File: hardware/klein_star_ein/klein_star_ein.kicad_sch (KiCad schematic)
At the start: 184 parts, among them J1 USB_A, J10 AudioJack3_Ground_Switch, J11 AudioJack3_Ground_Switch, J12 AudioJack3_Ground_Switch, J2 DB15_Female_HighDensity_Mount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, J3 Bus_PCI_Express_x1, J4 1367073-1, J5 RJ45_LED_Shielded, J6 USB_C_Receptacle, J7 MEM2051-00-195-00-A, J8 AudioJack3_Ground_Switch, J9 AudioJack3_Ground_Switch, U1 ECP5UM25, U10 SN74ALVC245PWR, U11 KSZ9021RL, U12 TUSB2036, U13 TPS2041B, U2 MT41K512M16, U3 MT41K512M16, U4 FT2232HQ, U5 W25Q128JVS, U6 USB3300-EZK, U7 USB3300-EZK, U8 SN74ALVC245PWR, U9 SN74ALVC245PWR

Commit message: ech
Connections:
- net +1V35: no longer U1.L14 (VCCIO3/-), U1.L15 (VCCIO3/-), U1.M15 (VCCIO3/-)
- net DRAM_ADDR_0: no longer U1.E17 (PR5B/RDQ8/-)
- net DRAM_ADDR_1: no longer U1.T18 (PR44D/RDQ44/-)
- net DRAM_ADDR_10: no longer U1.U16 (PR47C/RDQ44/LRC_GPLL0T_IN)
- net DRAM_ADDR_11: no longer U1.R17 (PR35D/RDQ32/-)
- net DRAM_ADDR_12: now also RN7.2 (R2.1); no longer RN8.4 (R4.1), U1.U18 (PR47A/RDQ44/-)
- net DRAM_ADDR_13: no longer U1.J16 (PR11D/RDQ8/-)
- net DRAM_ADDR_14: now also RN6.4 (R4.1); no longer RN6.3 (R3.1), U1.L17 (PR29B/RDQ32/-)
- net DRAM_ADDR_15: now also RN8.4 (R4.1); no longer RN7.1 (R1.1), U1.U17 (PR47B/RDQ44/-)
- net DRAM_ADDR_3: no longer U1.E16 (PR2C/RDQ8/-)
- net DRAM_ADDR_4: no longer U1.R16 (PR35C/RDQ32/-)
- net DRAM_ADDR_6: no longer U1.L18 (PR29C/RDQ32/GR_PCLK3_1)
- net DRAM_ADDR_8: now also RN6.3 (R3.1); no longer RN6.4 (R4.1), U1.L16 (PR29A/RDQ32/GR_PCLK3_0)
- net DRAM_ADDR_9: no longer U1.J17 (PR11C/RDQ8/-)
- net DRAM_ADDR_BA0: no longer U1.D17 (PR2B/RDQ8/S0_IN)
- net DRAM_ADDR_BA1: now also RN7.1 (R1.1); no longer RN7.2 (R2.1), U1.T17 (PR47D/RDQ44/LRC_GPLL0C_IN)
- net DRAM_ADDR_BA2: no longer U1.D18 (PR5A/RDQ8/-)
- net DRAM_DATA_10: now also U1.H5 (PL20C/LDQ20/GR_PCLK7_0)
- net DRAM_DATA_11: now also U1.E1 (PL17D/LDQ20/-)
- net DRAM_DATA_12: now also U1.G3 (PL23A/LDQ20/PCLKT7_1)
- net DRAM_DATA_13: now also U1.E2 (PL23D/LDQ20/PCLKC7_0)
- net DRAM_DATA_14: now also U1.F3 (PL23B/LDQ20/PCLKC7_1)
- net DRAM_DATA_15: now also U1.F2 (PL23C/LDQ20/PCLKT7_0)
- net DRAM_DATA_16: now also U1.F18 (PR5D/RDQ8/-)
- net DRAM_DATA_17: now also U1.D18 (PR5A/RDQ8/-)
- net DRAM_DATA_18: now also U1.F16 (PR2D/RDQ8/-)
- net DRAM_DATA_19: now also U1.D17 (PR2B/RDQ8/S0_IN)
- net DRAM_DATA_20: now also U1.G16 (PR8C/RDQ8/-)
- net DRAM_DATA_21: now also U1.E16 (PR2C/RDQ8/-)
- net DRAM_DATA_22: now also U1.E17 (PR5B/RDQ8/-)
- net DRAM_DATA_23: now also U1.E18 (PR5C/RDQ8/-)
- net DRAM_DATA_24: now also U1.G20 (PR17D/RDQ20/-)
- net DRAM_DATA_25: now also U1.J20 (PR23C/RDQ20/PCLKT2_0)
- net DRAM_DATA_26: now also U1.F19 (PR17B/RDQ20/-)
- net DRAM_DATA_27: now also U1.K20 (PR23D/RDQ20/PCLKC2_0)
- net DRAM_DATA_28: now also U1.E19 (PR14D/RDQ20/-)
- net DRAM_DATA_29: now also U1.K19 (PR23B/RDQ20/PCLKC2_1)
- net DRAM_DATA_30: now also U1.D19 (PR14B/RDQ20/-)
- net DRAM_DATA_31: now also U1.J19 (PR23A/RDQ20/PCLKT2_1)
- net DRAM_DATA_4: now also U1.B4 (PL5B/LDQ8/-)
- net DRAM_DATA_5: now also U1.C4 (PL5A/LDQ8/-)
- net DRAM_DATA_6: now also U1.B3 (PL5D/LDQ8/-)
- net DRAM_DATA_7: now also U1.C5 (PL2D/LDQ8/-)
- net DRAM_DATA_8: now also U1.H3 (PL20D/LDQ20/-)
- net DRAM_DM2: now also U1.C18 (PR2A/RDQ8/-)
- net DRAM_DM3: now also U1.J18 (PR20C/RDQ20/GR_PCLK2_0)
- net DRAM_DQS0_N: now also U1.D5 (PL8B/LDQSN8/-); no longer U1.R18 (PR44B/RDQSN44/-)
- net DRAM_DQS0_P: now also U1.E4 (PL8A/LDQS8/-); no longer U1.T19 (PR44A/RDQS44/-)
- net DRAM_DQS1_N: now also U1.G5 (PL20B/LDQSN20/-); no longer U1.M17 (PR32B/RDQSN32/-)
- net DRAM_DQS1_P: now also U1.H4 (PL20A/LDQS20/GR_PCLK7_1); no longer U1.N16 (PR32A/RDQS32/-)
- net DRAM_DQS2_N: now also U1.G18 (PR8B/RDQSN8/-)
- net DRAM_DQS2_P: now also U1.F17 (PR8A/RDQS8/-)
- net DRAM_DQS3_N: now also U1.H20 (PR20B/RDQSN20/-)
- net DRAM_DQS3_P: now also U1.G19 (PR20A/RDQS20/GR_PCLK2_1)
- net DRAM_nCS: no longer U1.C20 (PR14A/RDQ20/-)
- net DRAM_nWE: no longer U1.C18 (PR2A/RDQ8/-)
- net FIFO_D0/RX: no longer U1.B3 (PL5D/LDQ8/-)
- net FIFO_D1/TX: no longer U1.A2 (PL14A/LDQ20/-)
- net FIFO_D2: no longer U1.B4 (PL5B/LDQ8/-)
- net FIFO_D3: no longer U1.A3 (PL5C/LDQ8/-)
- net FIFO_D4: no longer U1.B5 (PL2C/LDQ8/-)
- net FIFO_D5: no longer U1.A4 (PL2A/LDQ8/-)
- net FIFO_D6: no longer U1.C5 (PL2D/LDQ8/-)
- net FIFO_D7: no longer U1.A5 (PL2B/LDQ8/-)
- net FIFO_WKUP: no longer U1.E5 (PL11C/LDQ8/-)
- net FIFO_nRD: no longer U1.D5 (PL8B/LDQSN8/-)
- net FIFO_nRXE: no longer U1.C4 (PL5A/LDQ8/-)
- net FIFO_nTXE: no longer U1.C3 (PL8C/LDQ8/-)
- net FIFO_nWR: no longer U1.D3 (PL8D/LDQ8/-)
- net USB_SLAVE_CLK: no longer U1.E4 (PL8A/LDQS8/-)
- net USB_SLAVE_CLKOUT: no longer U1.F5 (PL11D/LDQ8/-)
- net USB_SLAVE_DATA0: no longer U1.B1 (PL14B/LDQ20/-)
- net USB_SLAVE_DATA1: no longer U1.B2 (PL14C/LDQ20/VREF1_7)
- net USB_SLAVE_DATA2: no longer U1.C1 (PL17A/LDQ20/-)
- net USB_SLAVE_DATA3: no longer U1.C2 (PL14D/LDQ20/-)
- net USB_SLAVE_DATA4: no longer U1.D1 (PL17B/LDQ20/-)
- net USB_SLAVE_DATA5: no longer U1.D2 (PL17C/LDQ20/-)
- net USB_SLAVE_DATA6: no longer U1.E1 (PL17D/LDQ20/-)
- net USB_SLAVE_DATA7: no longer U1.E2 (PL23D/LDQ20/PCLKC7_0)
- net USB_SLAVE_DIR: no longer U1.F4 (PL11A/LDQ8/-)
- net USB_SLAVE_NXT: no longer U1.F3 (PL23B/LDQ20/PCLKC7_1)
- net USB_SLAVE_RESET: no longer U1.E3 (PL11B/LDQ8/-)
- net USB_SLAVE_STP: no longer U1.G3 (PL23A/LDQ20/PCLKT7_1)
- net at U1.A12 (PT40A/-): now also U1.A13 (PT40B/-), U1.A14 (PT47A/-), U1.A16 (PT56A/-), U1.A17 (PT62A/-), U1.A18 (PT65A/-), U1.A19 (PT67A/-), U1.B12 (PT35A/PCLKT1_0), U1.B13 (PT42A/-), U1.B15 (PT51A/-), U1.B16 (PT56B/-), U1.B17 (PT60A/-), U1.B18 (PT62B/-), U1.B19 (PT65B/-), U1.B20 (PT67B/-), U1.C12 (PT35B/PCLKC1_0), U1.C13 (PT42B/-), U1.C14 (PT47B/-), U1.C15 (PT51B/-), U1.C16 (PT58A/-), U1.C17 (PT60B/-), U1.D11 (PT33A/PCLKT1_1), U1.D12 (PT38A/GR_PCLK1_0), U1.D13 (PT44A/-), U1.D14 (PT49A/-), U1.D15 (PT53A/-), U1.D16 (PT58B/-), U1.E11 (PT33B/PCLKC1_1), U1.E12 (PT38B/GR_PCLK1_1), U1.E13 (PT44B/-), U1.E14 (PT49B/-), U1.E15 (PT53B/-)
- now unconnected: U1.H6 (VCCIO7/-), U1.H7 (VCCIO7/-), U1.J6 (VCCIO7/-)
- no-connect marks 61 -> 63
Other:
- moved on the sheet: RN3A, RN3B, RN3C, RN3D, RN6C, RN6D, RN7A, RN7B, RN8D, U1A, U1B, U1D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

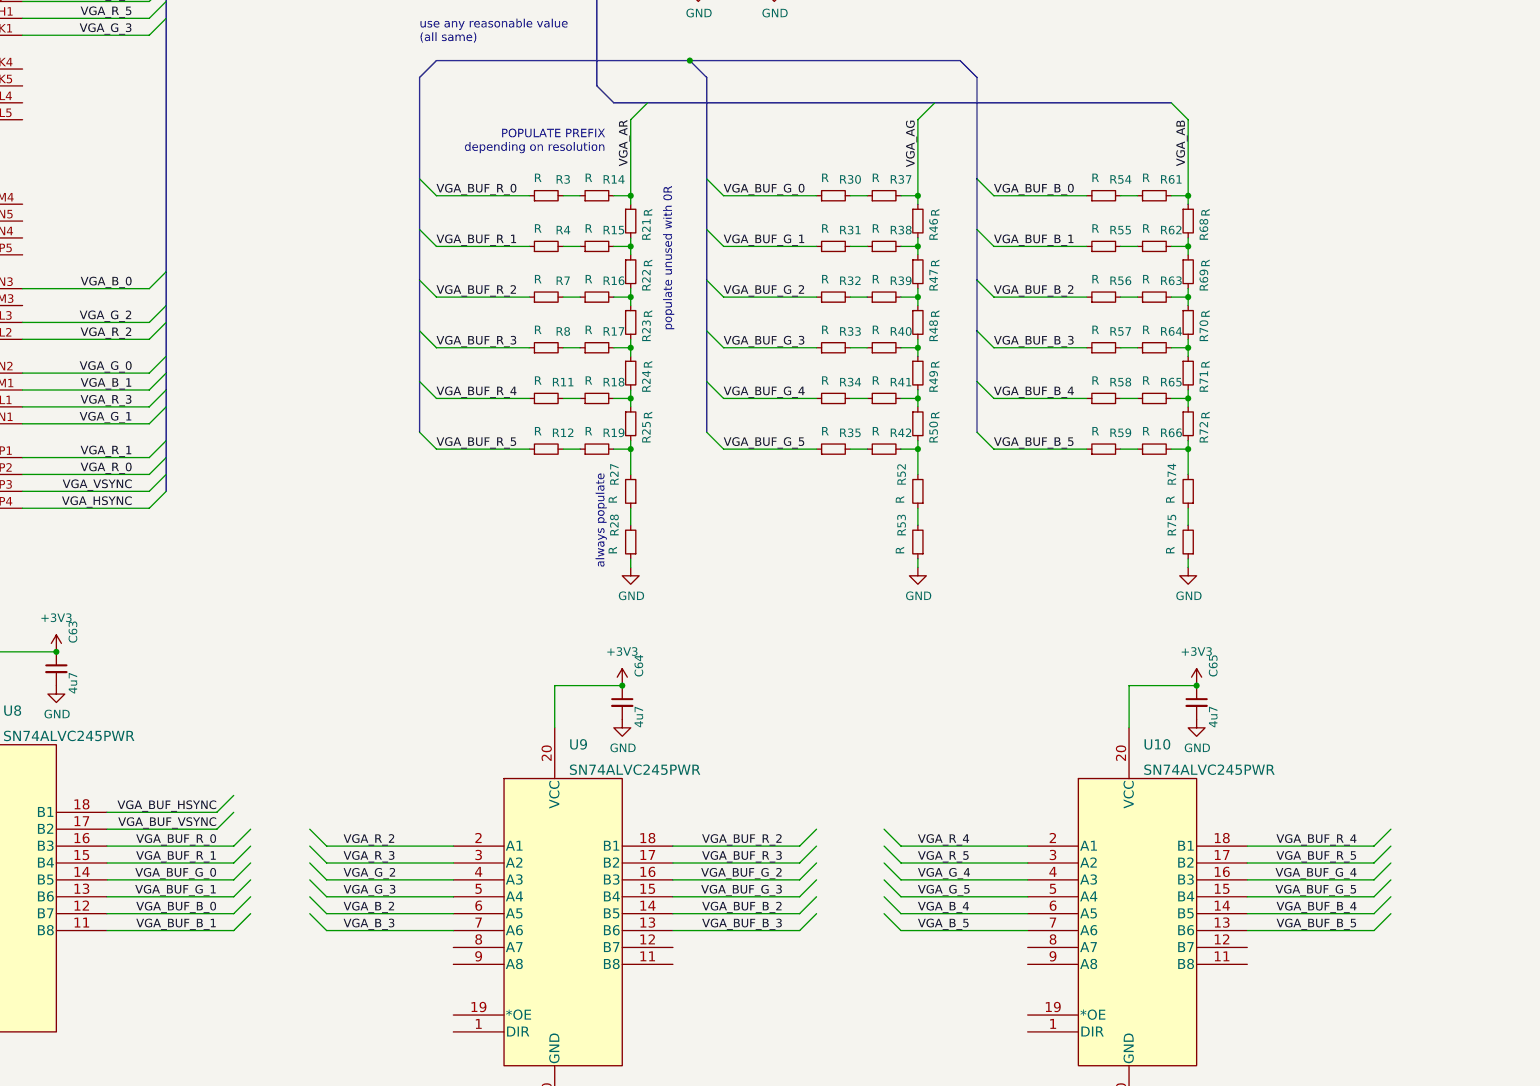
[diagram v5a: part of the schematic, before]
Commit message: changed VGA drivers to use resistor networks
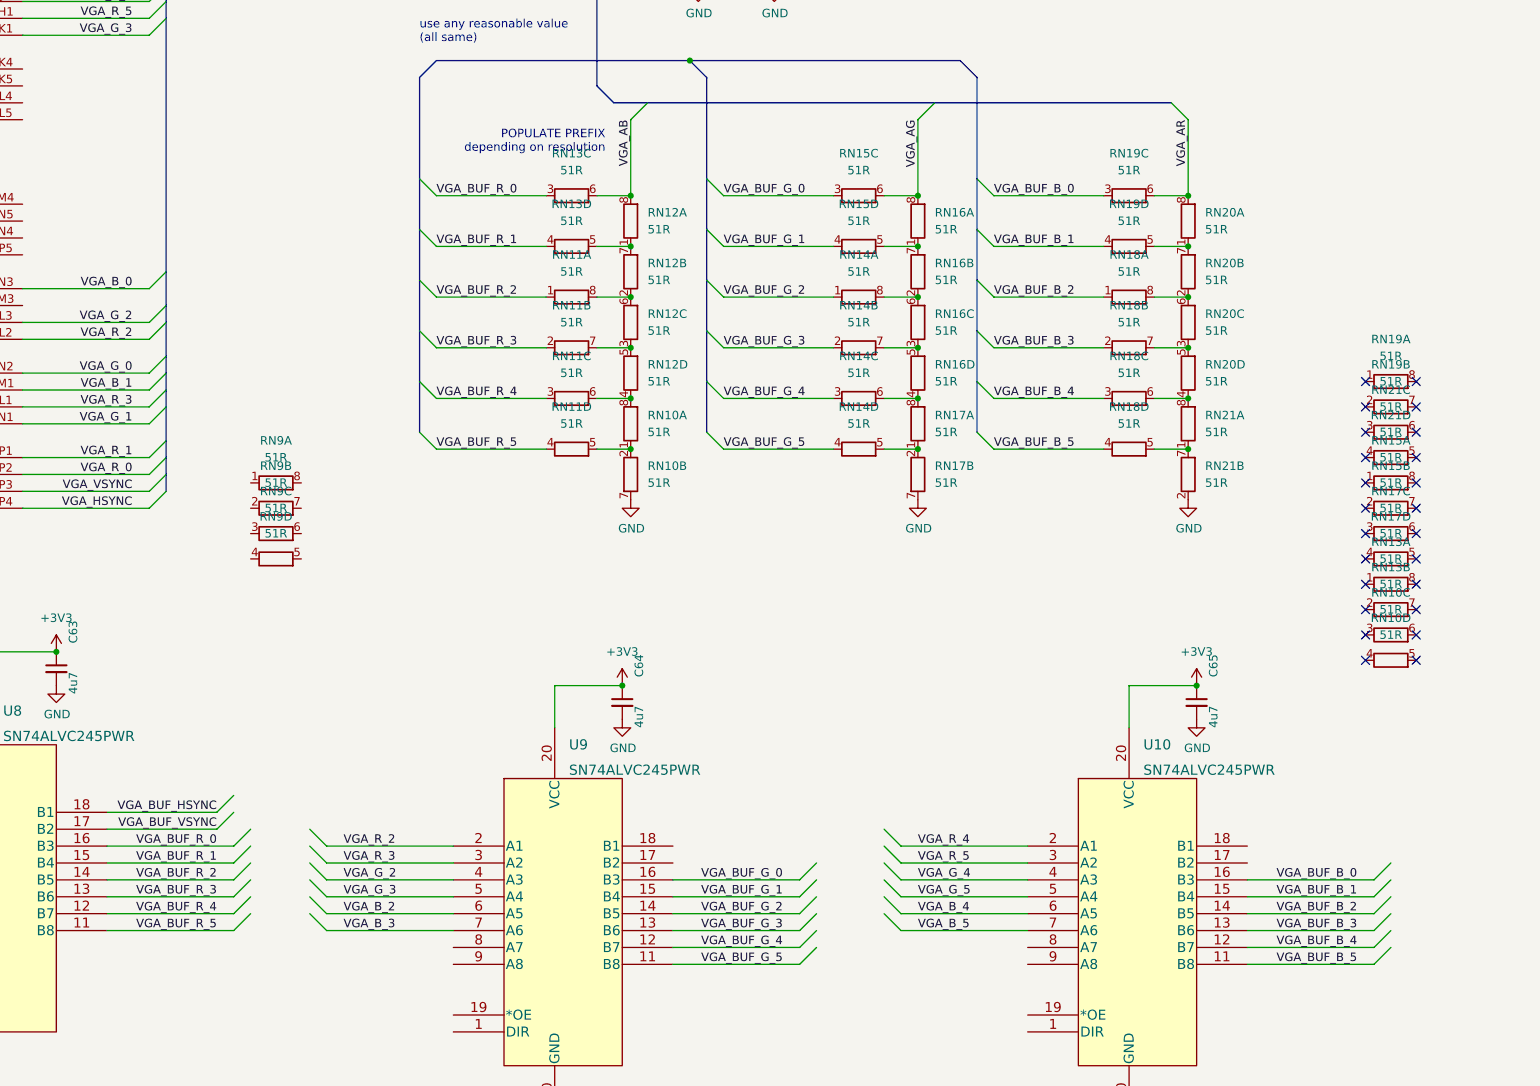
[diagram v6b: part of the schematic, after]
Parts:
- removed R11, R12, R14, R15, R16, R17, R18, R19, R21, R22, R23, R24, R25, R27, R28, R3, R30, R31, R32, R33, R34, R35, R37, R38, R39, R4, R40, R41, R42, R46, R47, R48, R49, R50, R52, R53, R54, R55, R56, R57, R58, R59, R61, R62, R63, R64, R65, R66, R68, R69, R7, R70, R71, R72, R74, R75, R8: R, Resistor_SMD:R_0402_1005Metric_Pad0.72x0.64mm_HandSolder, symbol Device:R_Small
- added RN10, RN11, RN12, RN13, RN14, RN15, RN16, RN17, RN18, RN20, RN9: 51R, symbol Device:R_Pack04_Split
- added RN19, RN21: 51R, Resistor_SMD:R_Array_Concave_4x0402, symbol Device:R_Pack04_Split
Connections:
- net GND: now also RN10.7 (R2.2), RN17.7 (R2.2), RN21.2 (R2.1)
- net VGA_AB: now also RN12.8 (R1.2), RN13.6 (R3.2)
- net VGA_AG: now also RN15.6 (R3.2), RN16.8 (R1.2)
- net VGA_AR: now also RN19.6 (R3.2), RN20.8 (R1.2)
- net VGA_BUF_B_0: now also U10.16 (B3), RN19.3 (R3.1); no longer U8.12 (B7)
- net VGA_BUF_B_1: now also U10.15 (B4), RN19.4 (R4.1); no longer U8.11 (B8)
- net VGA_BUF_B_2: now also U10.14 (B5), RN18.1 (R1.1); no longer U9.14 (B5)
- net VGA_BUF_B_3: now also U10.13 (B6), RN18.2 (R2.1); no longer U9.13 (B6)
- net VGA_BUF_B_4: now also U10.12 (B7), RN18.3 (R3.1); no longer U10.14 (B5)
- net VGA_BUF_B_5: now also U10.11 (B8), RN18.4 (R4.1); no longer U10.13 (B6)
- net VGA_BUF_G_0: now also U9.16 (B3), RN15.3 (R3.1); no longer U8.14 (B5)
- net VGA_BUF_G_1: now also U9.15 (B4), RN15.4 (R4.1); no longer U8.13 (B6)
- net VGA_BUF_G_2: now also U9.14 (B5), RN14.1 (R1.1); no longer U9.16 (B3)
- net VGA_BUF_G_3: now also U9.13 (B6), RN14.2 (R2.1); no longer U9.15 (B4)
- net VGA_BUF_G_4: now also U9.12 (B7), RN14.3 (R3.1); no longer U10.16 (B3)
- net VGA_BUF_G_5: now also U9.11 (B8), RN14.4 (R4.1); no longer U10.15 (B4)
- net VGA_BUF_R_0: now also RN13.3 (R3.1)
- net VGA_BUF_R_1: now also RN13.4 (R4.1)
- net VGA_BUF_R_2: now also U8.14 (B5), RN11.1 (R1.1); no longer U9.18 (B1)
- net VGA_BUF_R_3: now also U8.13 (B6), RN11.2 (R2.1); no longer U9.17 (B2)
- net VGA_BUF_R_4: now also U8.12 (B7), RN11.3 (R3.1); no longer U10.18 (B1)
- net VGA_BUF_R_5: now also U8.11 (B8), RN11.4 (R4.1); no longer U10.17 (B2)
- new net: RN18.5 (R4.2), RN21.1 (R1.1), RN21.7 (R2.2)
- new net: RN18.6 (R3.2), RN20.4 (R4.1), RN21.8 (R1.2)
- new net: RN14.6 (R3.2), RN16.4 (R4.1), RN17.8 (R1.2)
- new net: RN18.8 (R1.2), RN20.2 (R2.1), RN20.6 (R3.2)
- new net: RN19.5 (R4.2), RN20.1 (R1.1), RN20.7 (R2.2)
- new net: RN11.8 (R1.2), RN12.2 (R2.1), RN12.6 (R3.2)
- new net: RN12.1 (R1.1), RN12.7 (R2.2), RN13.5 (R4.2)
- new net: RN18.7 (R2.2), RN20.3 (R3.1), RN20.5 (R4.2)
- new net: RN11.7 (R2.2), RN12.3 (R3.1), RN12.5 (R4.2)
- new net: RN10.1 (R1.1), RN10.2 (R2.1), RN11.5 (R4.2)
- new net: RN14.7 (R2.2), RN16.3 (R3.1), RN16.5 (R4.2)
- new net: RN14.8 (R1.2), RN16.2 (R2.1), RN16.6 (R3.2)
- new net: RN14.5 (R4.2), RN17.1 (R1.1), RN17.2 (R2.1)
- new net: RN10.8 (R1.2), RN11.6 (R3.2), RN12.4 (R4.1)
- new net: RN15.5 (R4.2), RN16.1 (R1.1), RN16.7 (R2.2)
- no-connect marks 63 -> 87
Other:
- note removed: "always populate"
- note removed: "populate unused with 0R"

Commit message: a
a
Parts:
- removed J5: RJ45_LED_Shielded, Connector_RJ:RJ45_Amphenol_RJHSE538X, symbol Connector:RJ45_LED_Shielded
- added J5: ARJM11C7-502-AB-ER2-T, footprints:ABRACON_ARJM11C7-502-AB-ER2-T, symbol ARJM11C7-502-AB-ER2-T:ARJM11C7-502-AB-ER2-T
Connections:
- net at U11.1 (TXRXP_A): now also J5.1 (TRD1+)
- net at U11.10 (TXRXP_C): now also J5.7 (TRD3+)
- net at U11.11 (TXRXM_C): now also J5.8 (TRD3-)
- net at U11.14 (TXRXP_D): now also J5.9 (TRD4+)
- net at U11.15 (TXRXM_D): now also J5.10 (TRD4-)
- net at U11.2 (TXRXM_A): now also J5.2 (TRD1-)
- net at U11.7 (TXRXP_B): now also J5.3 (TRD2+)
- net at U11.8 (TXRXM_B): now also J5.4 (TRD2-)
- new net: J5.S1 (SHIELD), J5.S2 (SHIELD)
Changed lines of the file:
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@@
     (stroke (width 0) (type solid) (color 0 0 0 0))
   )
+  (wire (pts (xy 764.54 477.52) (xy 787.4 477.52))
+    (stroke (width 0) (type default) (color 0 0 0 0))
+  )
   (wire (pts (xy 153.67 523.24) (xy 172.72 523.24))
     (stroke (width 0) (type default) (color 0 0 0 0))
@@
     (stroke (width 0) (type solid) (color 0 0 0 0))
   )
+  (wire (pts (xy 764.54 472.44) (xy 787.4 472.44))
+    (stroke (width 0) (type default) (color 0 0 0 0))
+  )
   (wire (pts (xy 1084.58 133.35) (xy 1115.06 133.35))
     (stroke (width 0) (type solid) (color 0 0 0 0))
@@
     (stroke (width 0) (type solid) (color 0 0 0 0))
   )
+  (wire (pts (xy 764.54 462.28) (xy 787.4 462.28))
+    (stroke (width 0) (type default) (color 0 0 0 0))
+  )
   (wire (pts (xy 1023.62 275.59) (xy 1050.29 275.59))
     (stroke (width 0) (type solid) (color 0 0 0 0))
@@
     (stroke (width 0) (type solid) (color 0 0 0 0))
   )
+  (wire (pts (xy 764.54 469.9) (xy 787.4 469.9))
+    (stroke (width 0) (type default) (color 0 0 0 0))
+  )
   (wire (pts (xy 976.63 149.86) (xy 976.63 153.67))
     (stroke (width 0) (type solid) (color 0 0 0 0))
@@
     (stroke (width 0) (type solid) (color 0 0 0 0))
   )
+  (wire (pts (xy 764.54 459.74) (xy 787.4 459.74))
+    (stroke (width 0) (type default) (color 0 0 0 0))
+  )
   (wire (pts (xy 107.95 234.95) (xy 107.95 241.3))
     (stroke (width 0) (type solid) (color 0 0 0 0))
@@
     (stroke (width 0) (type solid) (color 0 0 0 0))
   )
+  (wire (pts (xy 764.54 467.36) (xy 787.4 467.36))
+    (stroke (width 0) (type default) (color 0 0 0 0))
+  )
   (bus (pts (xy 1021.08 252.73) (xy 1021.08 255.27))
     (stroke (width 0) (type solid) (color 0 0 0 0))
@@
     (stroke (width 0) (type solid) (color 0 0 0 0))
   )
+  (wire (pts (xy 764.54 464.82) (xy 787.4 464.82))
+    (stroke (width 0) (type default) (color 0 0 0 0))
+  )
   (bus (pts (xy 175.26 523.24) (xy 175.26 525.78))
     (stroke (width 0) (type default) (color 0 0 0 0))
@@
     (stroke (width 0) (type solid) (color 0 0 0 0))
   )
+  (wire (pts (xy 764.54 474.98) (xy 787.4 474.98))
+    (stroke (width 0) (type default) (color 0 0 0 0))
+  )
   (polyline (pts (xy 284.48 57.15) (xy 284.48 260.35))
     (stroke (width 0) (type dash) (color 0 0 0 0))
@@
     (pin "2")
   )
-  (symbol (lib_id "Connector:RJ45_LED_Shielded") (at 866.14 458.47 0) (unit 1)
-    (in_bom yes) (on_board yes) (fields_autoplaced)
-    (property "Reference" "J5" (id 0) (at 866.14 440.69 0))
-    (property "Value" "RJ45_LED_Shielded" (id 1) (at 866.14 443.23 0))
-    (property "Footprint" "Connector_RJ:RJ45_Amphenol_RJHSE538X" (id 2) (at 866.14 457.835 90)
-      (effects (font (size 1.27 1.27)) hide)
-    )
-    (property "Datasheet" "~" (id 3) (at 866.14 457.835 90)
-      (effects (font (size 1.27 1.27)) hide)
-    )
-    (pin "1")
-    (pin "10")
-    (pin "11")
-    (pin "12")
-    (pin "2")
-    (pin "3")
-    (pin "4")
-    (pin "5")
-    (pin "6")
-    (pin "7")
-    (pin "8")
-    (pin "9")
-    (pin "SH")
-  )
   (symbol (lib_id "Device:R_Pack04_Split") (at 328.93 538.48 0) (unit 2)
     (in_bom yes) (on_board yes) (fields_autoplaced)
@@
     (pin "2")
   )
+  (symbol (lib_id "ARJM11C7-502-AB-ER2-T:ARJM11C7-502-AB-ER2-T") (at 802.64 477.52 0) (unit 1)
+    (in_bom yes) (on_board yes) (fields_autoplaced)
+    (property "Reference" "J5" (id 0) (at 814.07 476.2499 0)
+      (effects (font (size 1.27 1.27)) (justify left))
+    )
+    (property "Value" "ARJM11C7-502-AB-ER2-T" (id 1) (at 814.07 478.7899 0)
+      (effects (font (size 1.27 1.27)) (justify left))
+    )
+    (property "Footprint" "footprints:ABRACON_ARJM11C7-502-AB-ER2-T" (id 2) (at 802.64 477.52 0)
+      (effects (font (size 1.27 1.27)) (justify left bottom) hide)
+    )
+    (property "Datasheet" "" (id 3) (at 802.64 477.52 0)
+      (effects (font (size 1.27 1.27)) (justify left bottom) hide)
+    )
+    (property "PARTREV" "04.22.2019" (id 4) (at 802.64 477.52 0)
+      (effects (font (size 1.27 1.27)) (justify left bottom) hide)
+    )
+    (property "STANDARD" "Manufacturer Recommendations" (id 5) (at 802.64 477.52 0)
+      (effects (font (size 1.27 1.27)) (justify left bottom) hide)
+    )
+    (property "MAXIMUM_PACKAGE_HEIGHT" "15.3mm" (id 6) (at 802.64 477.52 0)
+      (effects (font (size 1.27 1.27)) (justify left bottom) hide)
+    )
+    (property "MANUFACTURER" "Abracon" (id 7) (at 802.64 477.52 0)
+      (effects (font (size 1.27 1.27)) (justify left bottom) hide)
+    )
+    (pin "1")
+    (pin "10")
+    (pin "2")
+    (pin "3")
+    (pin "4")
+    (pin "5")
+    (pin "6")
+    (pin "7")
+    (pin "8")
+    (pin "9")
+    (pin "L1")
+    (pin "L2")
+    (pin "L3")
+    (pin "L4")
+    (pin "S1")
+    (pin "S2")
+  )
   (symbol (lib_id "power:GND") (at 96.52 154.94 0) (unit 1)
     (in_bom yes) (on_board yes)
@@
       (reference "J4") (unit 1) (value "1367073-1") (footprint "Connector:Connector_SFP_and_Cage")
     )
-    (path "/b1e40bbe-2558-469b-868d-b5f4f3aa37ac"
-      (reference "J5") (unit 1) (value "RJ45_LED_Shielded") (footprint "Connector_RJ:RJ45_Amphenol_RJHSE538X")
+    (path "/cf1fc535-27af-4de2-b16d-f5136377d6da"
+      (reference "J5") (unit 1) (value "ARJM11C7-502-AB-ER2-T") (footprint "footprints:ABRACON_ARJM11C7-502-AB-ER2-T")
     )
     (path "/ebc8e5e2-c4b1-4170-a57d-73ff1b106a16"
